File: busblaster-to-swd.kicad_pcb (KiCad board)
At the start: 2 copper layers, 22 x 35 mm, 6 parts, among them J101 CONN_02X10, J102 Tag Connect, J103 CONN_02X05

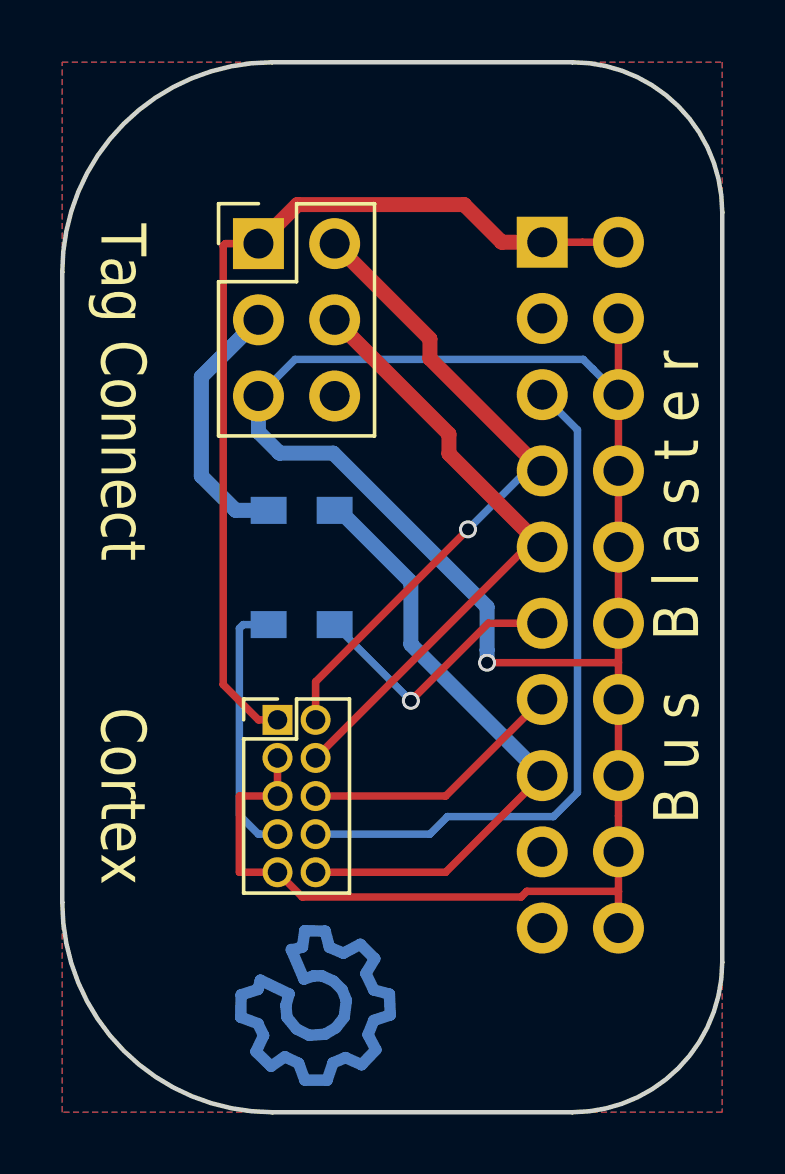
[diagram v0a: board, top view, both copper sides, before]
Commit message: Add SWCLK pullup resistor footprint
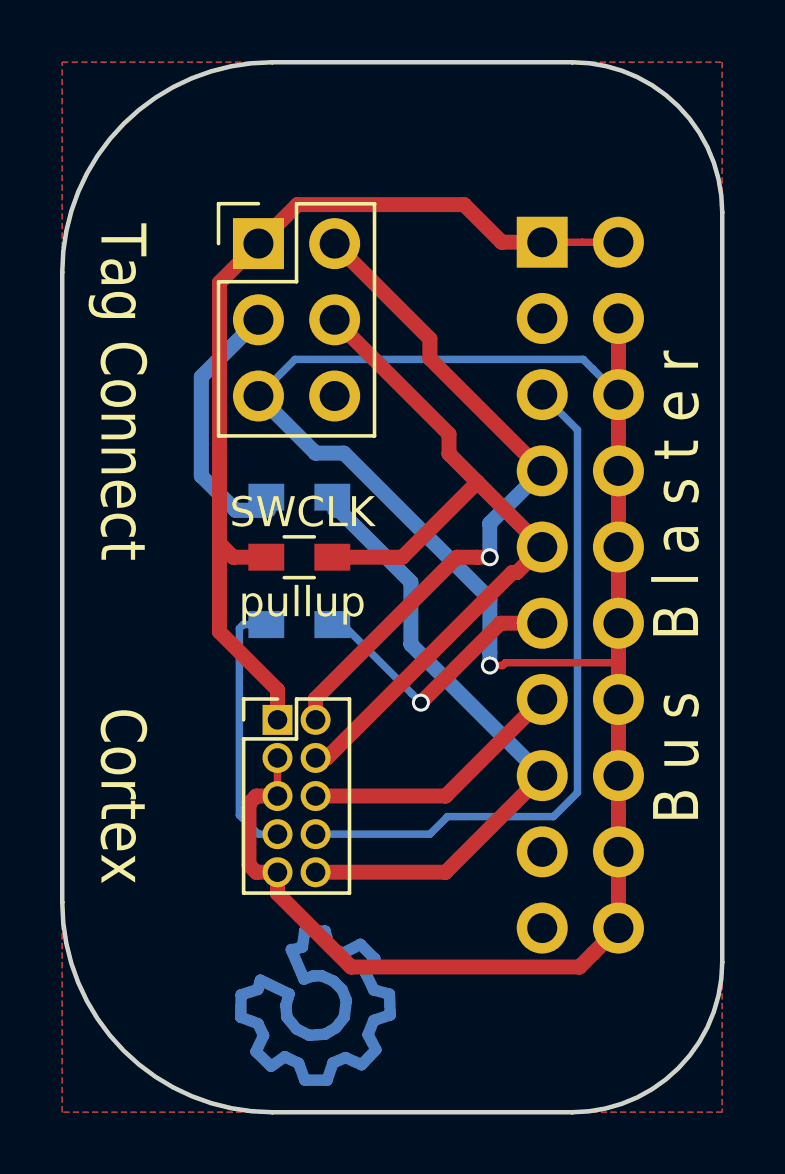
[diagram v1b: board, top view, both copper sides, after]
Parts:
- added R101: 1k, Resistors_SMD:R_0603_HandSoldering, F.Cu at (130.9, 116.5)
- moved JP101 0.44 mm to (130.9, 114.5)
- moved JP102 0.08 mm to (130.9, 118.7)
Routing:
- net /TCK/SWCLK: track 21.6 -> 28.0 mm
- net /TMS/SWDIO: track 22.2 -> 23.0 mm
- net /Vtarget: track 31.2 -> 32.0 mm
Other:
- board text added: "SWCLK"
- board text added: "pullup"

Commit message: Updated layout and included gerbers as ordered
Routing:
- net /GND: track 69.4 -> 77.9 mm, vias 1 -> 2
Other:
- board text added: "ARM SWD"
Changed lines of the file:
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@@
   (general
     (links 28)
-    (no_connects 2)
-    (area 122.924999 99.924999 145.075001 135.075001)
+    (no_connects 0)
+    (area 117.926315 99.924999 145.303334 136.812478)
     (thickness 1.6)
-    (drawings 22)
-    (tracks 99)
+    (drawings 23)
+    (tracks 105)
     (zones 0)
     (modules 7)
@@
   )
   (setup
-    (last_trace_width 0.5)
+    (last_trace_width 0.25)
     (user_trace_width 0.25)
     (user_trace_width 0.5)
@@
     (pad_drill 0.762)
     (pad_to_mask_clearance 0.2)
-    (aux_axis_origin 0 0)
+    (aux_axis_origin 123 135)
+    (grid_origin 123 135)
     (visible_elements FFFEFF7F)
     (pcbplotparams
-      (layerselection 0x00030_80000001)
-      (usegerberextensions false)
+      (layerselection 0x010f0_80000001)
+      (usegerberextensions true)
       (excludeedgelayer true)
       (linewidth 0.100000)
@@
       (outputformat 1)
       (mirror false)
-      (drillshape 1)
+      (drillshape 0)
       (scaleselection 1)
-      (outputdirectory ""))
+      (outputdirectory gerbers/))
   )
   (net 0 "")
@@
     )
   )
+  (gr_text "ARM SWD" (at 134 132) (layer F.SilkS)
+    (effects (font (size 1.5 1.5) (thickness 0.3)))
+  )
   (gr_text pullup (at 131 118) (layer F.SilkS)
     (effects (font (size 1 1) (thickness 0.15)))
@@
   (segment (start 141.54 106) (end 140.337919 106) (width 0.25) (layer F.Cu) (net 1))
   (segment (start 140.337919 106) (end 139 106) (width 0.25) (layer F.Cu) (net 1))
+  (segment (start 135 114) (end 134 114) (width 0.25) (layer B.Cu) (net 2))
+  (segment (start 130 113) (end 134 113) (width 0.25) (layer F.Cu) (net 2))
+  (segment (start 134 113) (end 135 114) (width 0.25) (layer F.Cu) (net 2))
+  (via (at 135 114) (size 0.6) (drill 0.4) (layers F.Cu B.Cu) (net 2))
+  (segment (start 129.54 112.54) (end 130 113) (width 0.25) (layer F.Cu) (net 2))
+  (segment (start 129.54 111.125) (end 129.54 112.54) (width 0.25) (layer F.Cu) (net 2))
   (segment (start 141.54 111.08) (end 141.54 108.54) (width 0.5) (layer F.Cu) (net 2))
   (segment (start 141.54 113.62) (end 141.54 111.08) (width 0.5) (layer F.Cu) (net 2))

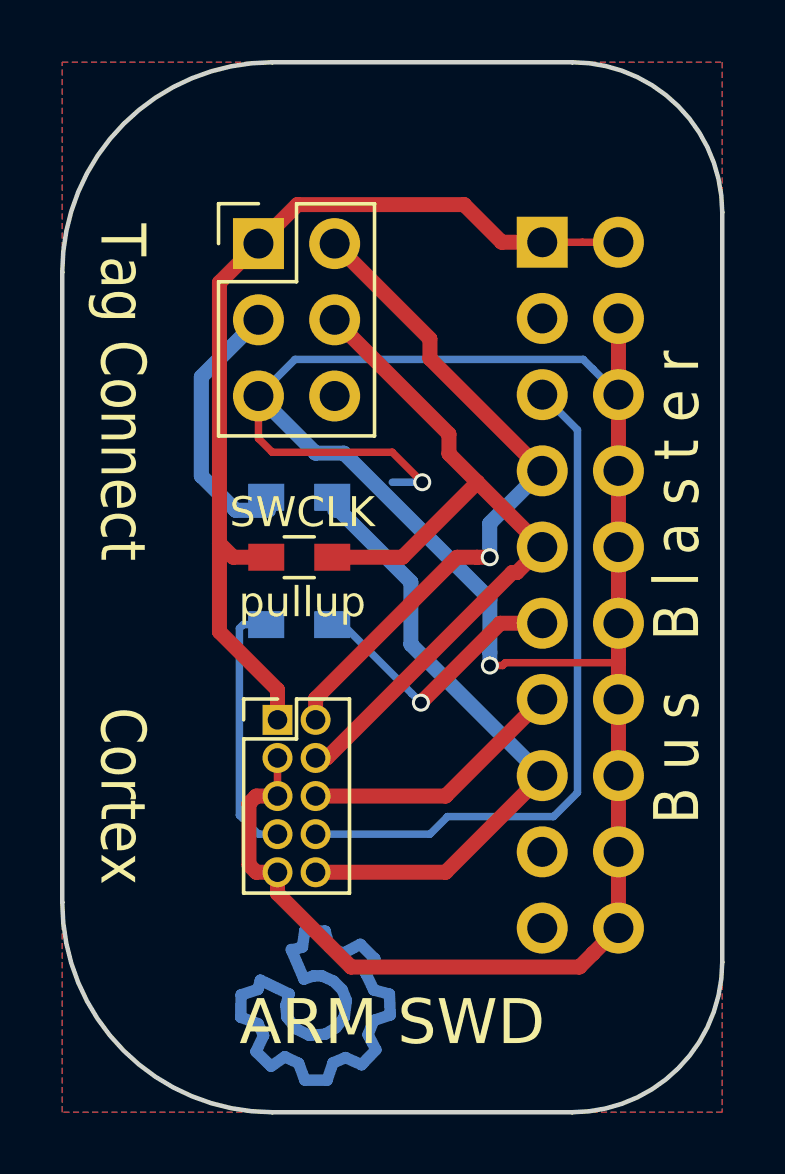
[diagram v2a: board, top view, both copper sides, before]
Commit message: Connect SWO to Tag-Connect, move SWCLK pullup
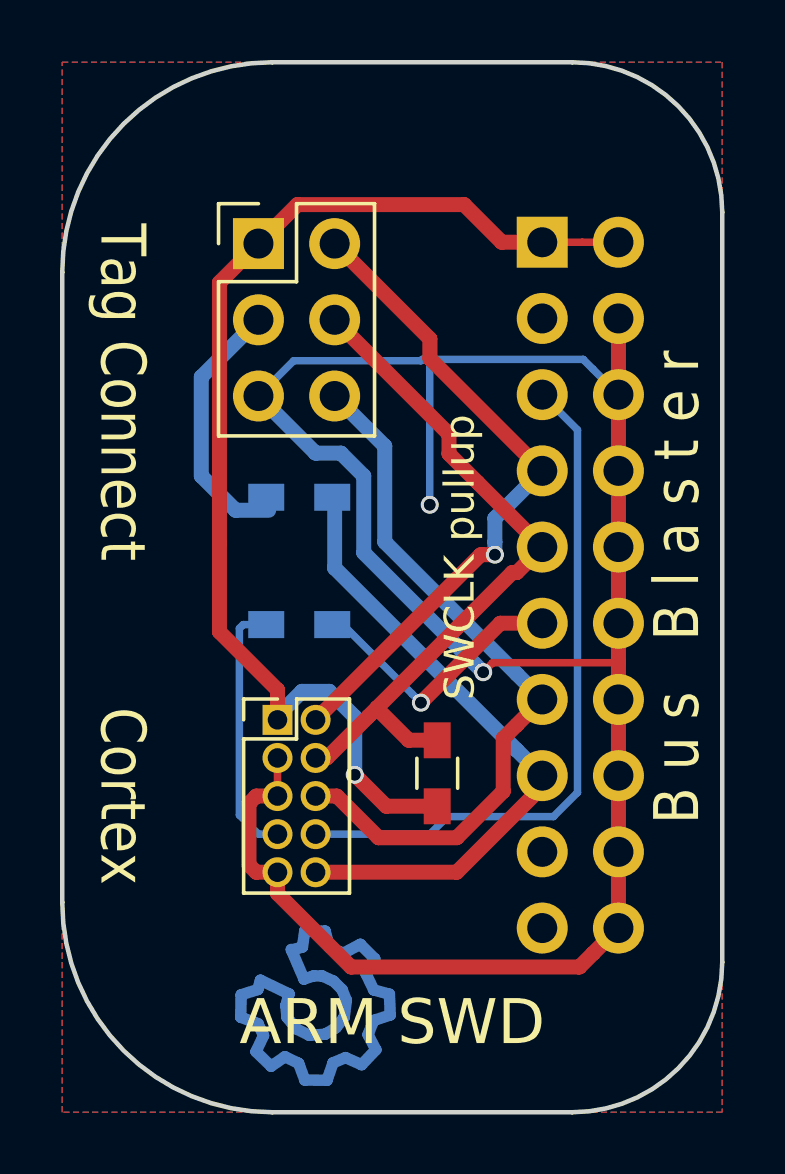
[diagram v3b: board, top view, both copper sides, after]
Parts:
- moved R101 8.54 mm to (135.5, 123.7), turned to 90 degrees
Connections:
- J102 pad 6: (no net) -> /SWO/TDO
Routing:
- net /SWO/TDO: track 8.89 -> 24.1 mm
- net /Vtarget: track 32.0 -> 38.8 mm, vias 0 -> 1
- net /TCK/SWCLK: track 28.0 -> 24.6 mm
- net /GND: track 77.9 -> 74.7 mm
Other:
- board text added: "SWCLK pullup"
- board text removed: "SWCLK"
- board text removed: "pullup"
